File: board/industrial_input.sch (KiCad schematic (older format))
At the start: 3 parts

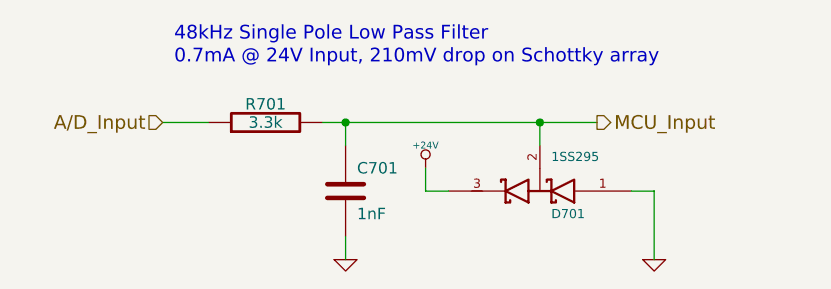
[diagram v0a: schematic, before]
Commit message: Selected Part Numbers for all Components
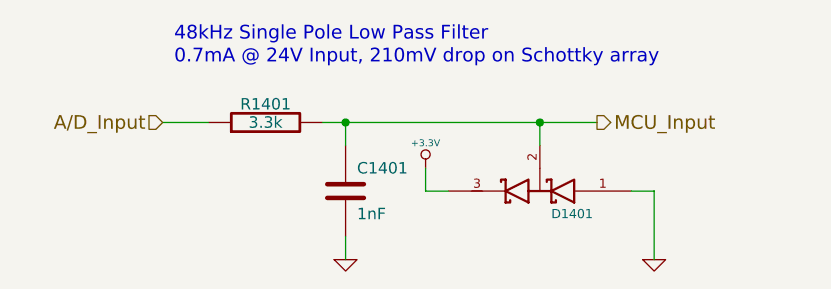
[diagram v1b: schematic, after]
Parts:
- C701: Part Number (none) -> CL10B102KB8NCNC
- D701: Part Number (none) -> 1SS295
- R701: Part Number (none) -> MCR50JZHJ332
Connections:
- net +24V renamed +3.3V
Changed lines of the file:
@@
 AR Path="/52F88315/52E6DE87" Ref="R1301"  Part="1"
 AR Path="/52F88319/52E6DE87" Ref="R1401"  Part="1"
-F 0 "R701" V 5480 3950 50  0000 C CNN
+F 0 "R1401" V 5480 3950 50  0000 C CNN
 F 1 "3.3k" V 5400 3950 50  0000 C CNN
 F 2 "" H 5400 3950 60  0000 C CNN
 F 3 "" H 5400 3950 60  0000 C CNN
+F 4 "MCR50JZHJ332" V 5400 3950 60  0001 C CNN "Part Number"
 	1    5400 3950
 	0    -1   -1   0
@@
 AR Path="/52F88315/52E6DEAB" Ref="C1301"  Part="1"
 AR Path="/52F88319/52E6DEAB" Ref="C1401"  Part="1"
-F 0 "C701" H 5800 4350 50  0000 L CNN
+F 0 "C1401" H 5800 4350 50  0000 L CNN
 F 1 "1nF" H 5800 4150 50  0000 L CNN
 F 2 "" H 5750 4250 60  0000 C CNN
 F 3 "" H 5750 4250 60  0000 C CNN
+F 4 "CL10B102KB8NCNC" H 5750 4250 60  0001 C CNN "Part Number"
 	1    5750 4250
 	1    0    0    -1
 $EndComp
 $Comp
-L GND #PWR0136
+L GND #PWR0141
 U 1 1 52E6DEC4
 P 5750 4550
-AR Path="/52F84966/52E6DEC4" Ref="#PWR0136"  Part="1"
-AR Path="/52F85705/52E6DEC4" Ref="#PWR0139"  Part="1"
-AR Path="/52F85B83/52E6DEC4" Ref="#PWR0142"  Part="1"
-AR Path="/52F85B87/52E6DEC4" Ref="#PWR0145"  Part="1"
-AR Path="/52F8830D/52E6DEC4" Ref="#PWR0148"  Part="1"
-AR Path="/52F88311/52E6DEC4" Ref="#PWR0151"  Part="1"
-AR Path="/52F88315/52E6DEC4" Ref="#PWR0154"  Part="1"
-AR Path="/52F88319/52E6DEC4" Ref="#PWR0157"  Part="1"
-F 0 "#PWR0136" H 5750 4550 30  0001 C CNN
+AR Path="/52F84966/52E6DEC4" Ref="#PWR0141"  Part="1"
+AR Path="/52F85705/52E6DEC4" Ref="#PWR0144"  Part="1"
+AR Path="/52F85B83/52E6DEC4" Ref="#PWR0147"  Part="1"
+AR Path="/52F85B87/52E6DEC4" Ref="#PWR0150"  Part="1"
+AR Path="/52F8830D/52E6DEC4" Ref="#PWR0153"  Part="1"
+AR Path="/52F88311/52E6DEC4" Ref="#PWR0156"  Part="1"
+AR Path="/52F88315/52E6DEC4" Ref="#PWR0159"  Part="1"
+AR Path="/52F88319/52E6DEC4" Ref="#PWR0162"  Part="1"
+F 0 "#PWR0162" H 5750 4550 30  0001 C CNN
 F 1 "GND" H 5750 4480 30  0001 C CNN
 F 2 "" H 5750 4550 60  0000 C CNN
@@
 $EndComp
 $Comp
-L +24V #PWR0137
-U 1 1 52E6DFBF
-P 6100 4150
-AR Path="/52F84966/52E6DFBF" Ref="#PWR0137"  Part="1"
-AR Path="/52F85705/52E6DFBF" Ref="#PWR0140"  Part="1"
-AR Path="/52F85B83/52E6DFBF" Ref="#PWR0143"  Part="1"
-AR Path="/52F85B87/52E6DFBF" Ref="#PWR0146"  Part="1"
-AR Path="/52F8830D/52E6DFBF" Ref="#PWR0149"  Part="1"
-AR Path="/52F88311/52E6DFBF" Ref="#PWR0152"  Part="1"
-AR Path="/52F88315/52E6DFBF" Ref="#PWR0155"  Part="1"
-AR Path="/52F88319/52E6DFBF" Ref="#PWR0158"  Part="1"
-F 0 "#PWR0137" H 6100 4100 20  0001 C CNN
-F 1 "+24V" H 6100 4250 30  0000 C CNN
-F 2 "" H 6100 4150 60  0000 C CNN
-F 3 "" H 6100 4150 60  0000 C CNN
-	1    6100 4150
-	1    0    0    -1
-$EndComp
-$Comp
-L GND #PWR0138
+L GND #PWR0142
 U 1 1 52E6DFEB
 P 7100 4550
-AR Path="/52F84966/52E6DFEB" Ref="#PWR0138"  Part="1"
-AR Path="/52F85705/52E6DFEB" Ref="#PWR0141"  Part="1"
-AR Path="/52F85B83/52E6DFEB" Ref="#PWR0144"  Part="1"
-AR Path="/52F85B87/52E6DFEB" Ref="#PWR0147"  Part="1"
-AR Path="/52F8830D/52E6DFEB" Ref="#PWR0150"  Part="1"
-AR Path="/52F88311/52E6DFEB" Ref="#PWR0153"  Part="1"
-AR Path="/52F88315/52E6DFEB" Ref="#PWR0156"  Part="1"
-AR Path="/52F88319/52E6DFEB" Ref="#PWR0159"  Part="1"
-F 0 "#PWR0138" H 7100 4550 30  0001 C CNN
+AR Path="/52F84966/52E6DFEB" Ref="#PWR0142"  Part="1"
+AR Path="/52F85705/52E6DFEB" Ref="#PWR0145"  Part="1"
+AR Path="/52F85B83/52E6DFEB" Ref="#PWR0148"  Part="1"
+AR Path="/52F85B87/52E6DFEB" Ref="#PWR0151"  Part="1"
+AR Path="/52F8830D/52E6DFEB" Ref="#PWR0154"  Part="1"
+AR Path="/52F88311/52E6DFEB" Ref="#PWR0157"  Part="1"
+AR Path="/52F88315/52E6DFEB" Ref="#PWR0160"  Part="1"
+AR Path="/52F88319/52E6DFEB" Ref="#PWR0163"  Part="1"
+F 0 "#PWR0163" H 7100 4550 30  0001 C CNN
 F 1 "GND" H 7100 4480 30  0001 C CNN
 F 2 "" H 7100 4550 60  0000 C CNN
@@
 AR Path="/52F88315/52E6E5BB" Ref="D1301"  Part="1"
 AR Path="/52F88319/52E6E5BB" Ref="D1401"  Part="1"
-F 0 "D701" H 6550 4350 40  0000 R CNN
-F 1 "1SS295" H 6550 4100 40  0000 R CNN
+F 0 "D1401" H 6550 4350 40  0000 R CNN
+F 1 "1SS295" H 6550 4100 40  0001 R CNN
 F 2 "" H 6600 4250 60  0000 C CNN
 F 3 "" H 6600 4250 60  0000 C CNN
+F 4 "1SS295" H 6600 4250 60  0001 C CNN "Part Number"
 	1    6600 4250
 	-1   0    0    1
@@
 Text Notes 5000 3700 0    60   ~ 0
 0.7mA @ 24V Input, 210mV drop on Schottky array
+$Comp
+L +3.3V #PWR0143
+U 1 1 5301839B
+P 6100 4150
+AR Path="/52F84966/5301839B" Ref="#PWR0143"  Part="1"
+AR Path="/52F85705/5301839B" Ref="#PWR0146"  Part="1"
+AR Path="/52F85B83/5301839B" Ref="#PWR0149"  Part="1"
+AR Path="/52F85B87/5301839B" Ref="#PWR0152"  Part="1"
+AR Path="/52F8830D/5301839B" Ref="#PWR0155"  Part="1"
+AR Path="/52F88311/5301839B" Ref="#PWR0158"  Part="1"
+AR Path="/52F88315/5301839B" Ref="#PWR0161"  Part="1"
+AR Path="/52F88319/5301839B" Ref="#PWR0164"  Part="1"
+F 0 "#PWR0164" H 6100 4110 30  0001 C CNN
+F 1 "+3.3V" H 6100 4260 30  0000 C CNN
+F 2 "" H 6100 4150 60  0000 C CNN
+F 3 "" H 6100 4150 60  0000 C CNN
+	1    6100 4150
+	1    0    0    -1
+$EndComp
 $EndSCHEMATC

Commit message: Digikey Number + Link
Added a digikey part number and link to all components.
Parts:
- C701: Digikey Number (none) -> 1276-1913-1-ND; Part Number CL10B102KB8NCNC -> (none)
- D701: Digikey Number (none) -> 1SS295(TE85LF)CT-ND; Part Number 1SS295 -> (none)
- R701: Digikey Number (none) -> RHM3.3KBGCT-ND; Part Number MCR50JZHJ332 -> (none)
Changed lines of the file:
@@
 F 1 "3.3k" V 5400 3950 50  0000 C CNN
 F 2 "" H 5400 3950 60  0000 C CNN
-F 3 "" H 5400 3950 60  0000 C CNN
-F 4 "MCR50JZHJ332" V 5400 3950 60  0001 C CNN "Part Number"
+F 3 "http://www.digikey.ca/product-detail/en/MCR50JZHJ332/RHM3.3KBGCT-ND/2291227" H 5400 3950 60  0001 C CNN
+F 4 "RHM3.3KBGCT-ND" H 6900 4550 60  0001 C CNN "Digikey Number"
 	1    5400 3950
 	0    -1   -1   0
@@
 F 1 "1nF" H 5800 4150 50  0000 L CNN
 F 2 "" H 5750 4250 60  0000 C CNN
-F 3 "" H 5750 4250 60  0000 C CNN
-F 4 "CL10B102KB8NCNC" H 5750 4250 60  0001 C CNN "Part Number"
+F 3 "http://www.digikey.ca/product-detail/en/CL10B102KB8NCNC/1276-1913-1-ND/3889999" H 5750 4250 60  0001 C CNN
+F 4 "1276-1913-1-ND" H 6900 4550 60  0001 C CNN "Digikey Number"
 	1    5750 4250
 	1    0    0    -1
@@
 F 1 "1SS295" H 6550 4100 40  0001 R CNN
 F 2 "" H 6600 4250 60  0000 C CNN
-F 3 "" H 6600 4250 60  0000 C CNN
-F 4 "1SS295" H 6600 4250 60  0001 C CNN "Part Number"
+F 3 "http://www.digikey.ca/product-detail/en/1SS295(TE85L,F)/1SS295(TE85LF)CT-ND/4304201" H 6600 4250 60  0001 C CNN
+F 4 "1SS295(TE85LF)CT-ND" H 6900 4550 60  0001 C CNN "Digikey Number"
 	1    6600 4250
 	-1   0    0    1

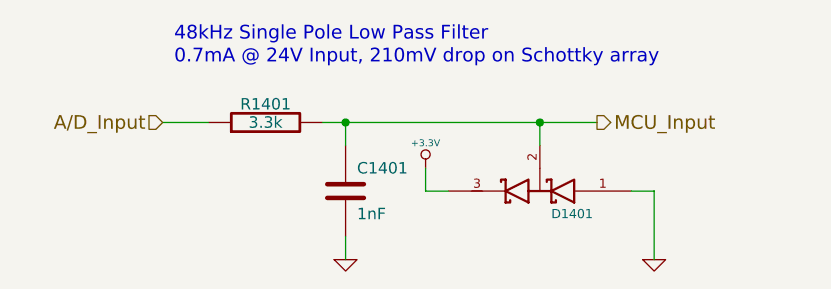
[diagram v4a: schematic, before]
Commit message: Removed PWR-GND, change footprint for a bunch of capacitors
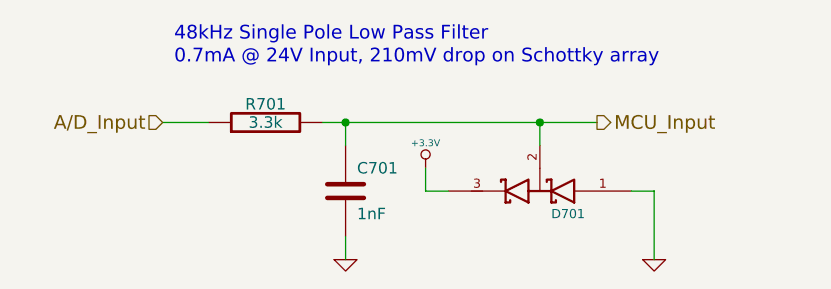
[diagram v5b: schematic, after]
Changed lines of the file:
@@
 AR Path="/52F88315/52E6DE87" Ref="R1301"  Part="1"
 AR Path="/52F88319/52E6DE87" Ref="R1401"  Part="1"
-F 0 "R1401" V 5480 3950 50  0000 C CNN
+F 0 "R701" V 5480 3950 50  0000 C CNN
 F 1 "3.3k" V 5400 3950 50  0000 C CNN
 F 2 "" H 5400 3950 60  0000 C CNN
@@
 AR Path="/52F88315/52E6DEAB" Ref="C1301"  Part="1"
 AR Path="/52F88319/52E6DEAB" Ref="C1401"  Part="1"
-F 0 "C1401" H 5800 4350 50  0000 L CNN
+F 0 "C701" H 5800 4350 50  0000 L CNN
 F 1 "1nF" H 5800 4150 50  0000 L CNN
 F 2 "" H 5750 4250 60  0000 C CNN
@@
 $EndComp
 $Comp
-L GND #PWR0141
+L GND #PWR0140
 U 1 1 52E6DEC4
 P 5750 4550
-AR Path="/52F84966/52E6DEC4" Ref="#PWR0141"  Part="1"
-AR Path="/52F85705/52E6DEC4" Ref="#PWR0144"  Part="1"
-AR Path="/52F85B83/52E6DEC4" Ref="#PWR0147"  Part="1"
-AR Path="/52F85B87/52E6DEC4" Ref="#PWR0150"  Part="1"
-AR Path="/52F8830D/52E6DEC4" Ref="#PWR0153"  Part="1"
-AR Path="/52F88311/52E6DEC4" Ref="#PWR0156"  Part="1"
-AR Path="/52F88315/52E6DEC4" Ref="#PWR0159"  Part="1"
-AR Path="/52F88319/52E6DEC4" Ref="#PWR0162"  Part="1"
-F 0 "#PWR0162" H 5750 4550 30  0001 C CNN
+AR Path="/52F84966/52E6DEC4" Ref="#PWR0140"  Part="1"
+AR Path="/52F85705/52E6DEC4" Ref="#PWR0143"  Part="1"
+AR Path="/52F85B83/52E6DEC4" Ref="#PWR0146"  Part="1"
+AR Path="/52F85B87/52E6DEC4" Ref="#PWR0149"  Part="1"
+AR Path="/52F8830D/52E6DEC4" Ref="#PWR0152"  Part="1"
+AR Path="/52F88311/52E6DEC4" Ref="#PWR0155"  Part="1"
+AR Path="/52F88315/52E6DEC4" Ref="#PWR0158"  Part="1"
+AR Path="/52F88319/52E6DEC4" Ref="#PWR0161"  Part="1"
+F 0 "#PWR0140" H 5750 4550 30  0001 C CNN
 F 1 "GND" H 5750 4480 30  0001 C CNN
 F 2 "" H 5750 4550 60  0000 C CNN
@@
 $EndComp
 $Comp
-L GND #PWR0142
+L GND #PWR0141
 U 1 1 52E6DFEB
 P 7100 4550
-AR Path="/52F84966/52E6DFEB" Ref="#PWR0142"  Part="1"
-AR Path="/52F85705/52E6DFEB" Ref="#PWR0145"  Part="1"
-AR Path="/52F85B83/52E6DFEB" Ref="#PWR0148"  Part="1"
-AR Path="/52F85B87/52E6DFEB" Ref="#PWR0151"  Part="1"
-AR Path="/52F8830D/52E6DFEB" Ref="#PWR0154"  Part="1"
-AR Path="/52F88311/52E6DFEB" Ref="#PWR0157"  Part="1"
-AR Path="/52F88315/52E6DFEB" Ref="#PWR0160"  Part="1"
-AR Path="/52F88319/52E6DFEB" Ref="#PWR0163"  Part="1"
-F 0 "#PWR0163" H 7100 4550 30  0001 C CNN
+AR Path="/52F84966/52E6DFEB" Ref="#PWR0141"  Part="1"
+AR Path="/52F85705/52E6DFEB" Ref="#PWR0144"  Part="1"
+AR Path="/52F85B83/52E6DFEB" Ref="#PWR0147"  Part="1"
+AR Path="/52F85B87/52E6DFEB" Ref="#PWR0150"  Part="1"
+AR Path="/52F8830D/52E6DFEB" Ref="#PWR0153"  Part="1"
+AR Path="/52F88311/52E6DFEB" Ref="#PWR0156"  Part="1"
+AR Path="/52F88315/52E6DFEB" Ref="#PWR0159"  Part="1"
+AR Path="/52F88319/52E6DFEB" Ref="#PWR0162"  Part="1"
+F 0 "#PWR0141" H 7100 4550 30  0001 C CNN
 F 1 "GND" H 7100 4480 30  0001 C CNN
 F 2 "" H 7100 4550 60  0000 C CNN
@@
 AR Path="/52F88315/52E6E5BB" Ref="D1301"  Part="1"
 AR Path="/52F88319/52E6E5BB" Ref="D1401"  Part="1"
-F 0 "D1401" H 6550 4350 40  0000 R CNN
+F 0 "D701" H 6550 4350 40  0000 R CNN
 F 1 "1SS295" H 6550 4100 40  0001 R CNN
 F 2 "" H 6600 4250 60  0000 C CNN
@@
 0.7mA @ 24V Input, 210mV drop on Schottky array
 $Comp
-L +3.3V #PWR0143
+L +3.3V #PWR0142
 U 1 1 5301839B
 P 6100 4150
-AR Path="/52F84966/5301839B" Ref="#PWR0143"  Part="1"
-AR Path="/52F85705/5301839B" Ref="#PWR0146"  Part="1"
-AR Path="/52F85B83/5301839B" Ref="#PWR0149"  Part="1"
-AR Path="/52F85B87/5301839B" Ref="#PWR0152"  Part="1"
-AR Path="/52F8830D/5301839B" Ref="#PWR0155"  Part="1"
-AR Path="/52F88311/5301839B" Ref="#PWR0158"  Part="1"
-AR Path="/52F88315/5301839B" Ref="#PWR0161"  Part="1"
-AR Path="/52F88319/5301839B" Ref="#PWR0164"  Part="1"
-F 0 "#PWR0164" H 6100 4110 30  0001 C CNN
+AR Path="/52F84966/5301839B" Ref="#PWR0142"  Part="1"
+AR Path="/52F85705/5301839B" Ref="#PWR0145"  Part="1"
+AR Path="/52F85B83/5301839B" Ref="#PWR0148"  Part="1"
+AR Path="/52F85B87/5301839B" Ref="#PWR0151"  Part="1"
+AR Path="/52F8830D/5301839B" Ref="#PWR0154"  Part="1"
+AR Path="/52F88311/5301839B" Ref="#PWR0157"  Part="1"
+AR Path="/52F88315/5301839B" Ref="#PWR0160"  Part="1"
+AR Path="/52F88319/5301839B" Ref="#PWR0163"  Part="1"
+F 0 "#PWR0142" H 6100 4110 30  0001 C CNN
 F 1 "+3.3V" H 6100 4260 30  0000 C CNN
 F 2 "" H 6100 4150 60  0000 C CNN

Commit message: Layed out in general where stuff is going to be located.
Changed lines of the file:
@@
 AR Path="/52F88315/52E6DE87" Ref="R1301"  Part="1"
 AR Path="/52F88319/52E6DE87" Ref="R1401"  Part="1"
-F 0 "R701" V 5480 3950 50  0000 C CNN
+F 0 "R1401" V 5480 3950 50  0000 C CNN
 F 1 "3.3k" V 5400 3950 50  0000 C CNN
 F 2 "" H 5400 3950 60  0000 C CNN
@@
 AR Path="/52F88315/52E6DEAB" Ref="C1301"  Part="1"
 AR Path="/52F88319/52E6DEAB" Ref="C1401"  Part="1"
-F 0 "C701" H 5800 4350 50  0000 L CNN
+F 0 "C1401" H 5800 4350 50  0000 L CNN
 F 1 "1nF" H 5800 4150 50  0000 L CNN
 F 2 "" H 5750 4250 60  0000 C CNN
@@
 $EndComp
 $Comp
-L GND #PWR0140
+L GND #PWR702
 U 1 1 52E6DEC4
 P 5750 4550
-AR Path="/52F84966/52E6DEC4" Ref="#PWR0140"  Part="1"
-AR Path="/52F85705/52E6DEC4" Ref="#PWR0143"  Part="1"
-AR Path="/52F85B83/52E6DEC4" Ref="#PWR0146"  Part="1"
-AR Path="/52F85B87/52E6DEC4" Ref="#PWR0149"  Part="1"
-AR Path="/52F8830D/52E6DEC4" Ref="#PWR0152"  Part="1"
-AR Path="/52F88311/52E6DEC4" Ref="#PWR0155"  Part="1"
-AR Path="/52F88315/52E6DEC4" Ref="#PWR0158"  Part="1"
-AR Path="/52F88319/52E6DEC4" Ref="#PWR0161"  Part="1"
-F 0 "#PWR0161" H 5750 4550 30  0001 C CNN
+AR Path="/52F84966/52E6DEC4" Ref="#PWR702"  Part="1"
+AR Path="/52F85705/52E6DEC4" Ref="#PWR802"  Part="1"
+AR Path="/52F85B83/52E6DEC4" Ref="#PWR902"  Part="1"
+AR Path="/52F85B87/52E6DEC4" Ref="#PWR1002"  Part="1"
+AR Path="/52F8830D/52E6DEC4" Ref="#PWR1102"  Part="1"
+AR Path="/52F88311/52E6DEC4" Ref="#PWR1202"  Part="1"
+AR Path="/52F88315/52E6DEC4" Ref="#PWR1302"  Part="1"
+AR Path="/52F88319/52E6DEC4" Ref="#PWR1402"  Part="1"
+F 0 "#PWR1402" H 5750 4550 30  0001 C CNN
 F 1 "GND" H 5750 4480 30  0001 C CNN
 F 2 "" H 5750 4550 60  0000 C CNN
@@
 $EndComp
 $Comp
-L GND #PWR0141
+L GND #PWR703
 U 1 1 52E6DFEB
 P 7100 4550
-AR Path="/52F84966/52E6DFEB" Ref="#PWR0141"  Part="1"
-AR Path="/52F85705/52E6DFEB" Ref="#PWR0144"  Part="1"
-AR Path="/52F85B83/52E6DFEB" Ref="#PWR0147"  Part="1"
-AR Path="/52F85B87/52E6DFEB" Ref="#PWR0150"  Part="1"
-AR Path="/52F8830D/52E6DFEB" Ref="#PWR0153"  Part="1"
-AR Path="/52F88311/52E6DFEB" Ref="#PWR0156"  Part="1"
-AR Path="/52F88315/52E6DFEB" Ref="#PWR0159"  Part="1"
-AR Path="/52F88319/52E6DFEB" Ref="#PWR0162"  Part="1"
-F 0 "#PWR0162" H 7100 4550 30  0001 C CNN
+AR Path="/52F84966/52E6DFEB" Ref="#PWR703"  Part="1"
+AR Path="/52F85705/52E6DFEB" Ref="#PWR803"  Part="1"
+AR Path="/52F85B83/52E6DFEB" Ref="#PWR903"  Part="1"
+AR Path="/52F85B87/52E6DFEB" Ref="#PWR1003"  Part="1"
+AR Path="/52F8830D/52E6DFEB" Ref="#PWR1103"  Part="1"
+AR Path="/52F88311/52E6DFEB" Ref="#PWR1203"  Part="1"
+AR Path="/52F88315/52E6DFEB" Ref="#PWR1303"  Part="1"
+AR Path="/52F88319/52E6DFEB" Ref="#PWR1403"  Part="1"
+F 0 "#PWR1403" H 7100 4550 30  0001 C CNN
 F 1 "GND" H 7100 4480 30  0001 C CNN
 F 2 "" H 7100 4550 60  0000 C CNN
@@
 AR Path="/52F88315/52E6E5BB" Ref="D1301"  Part="1"
 AR Path="/52F88319/52E6E5BB" Ref="D1401"  Part="1"
-F 0 "D701" H 6550 4350 40  0000 R CNN
+F 0 "D1401" H 6550 4350 40  0000 R CNN
 F 1 "1SS295" H 6550 4100 40  0001 R CNN
 F 2 "" H 6600 4250 60  0000 C CNN
@@
 0.7mA @ 24V Input, 210mV drop on Schottky array
 $Comp
-L +3.3V #PWR0142
+L +3.3V #PWR701
 U 1 1 5301839B
 P 6100 4150
-AR Path="/52F84966/5301839B" Ref="#PWR0142"  Part="1"
-AR Path="/52F85705/5301839B" Ref="#PWR0145"  Part="1"
-AR Path="/52F85B83/5301839B" Ref="#PWR0148"  Part="1"
-AR Path="/52F85B87/5301839B" Ref="#PWR0151"  Part="1"
-AR Path="/52F8830D/5301839B" Ref="#PWR0154"  Part="1"
-AR Path="/52F88311/5301839B" Ref="#PWR0157"  Part="1"
-AR Path="/52F88315/5301839B" Ref="#PWR0160"  Part="1"
-AR Path="/52F88319/5301839B" Ref="#PWR0163"  Part="1"
-F 0 "#PWR0163" H 6100 4110 30  0001 C CNN
+AR Path="/52F84966/5301839B" Ref="#PWR701"  Part="1"
+AR Path="/52F85705/5301839B" Ref="#PWR801"  Part="1"
+AR Path="/52F85B83/5301839B" Ref="#PWR901"  Part="1"
+AR Path="/52F85B87/5301839B" Ref="#PWR1001"  Part="1"
+AR Path="/52F8830D/5301839B" Ref="#PWR1101"  Part="1"
+AR Path="/52F88311/5301839B" Ref="#PWR1201"  Part="1"
+AR Path="/52F88315/5301839B" Ref="#PWR1301"  Part="1"
+AR Path="/52F88319/5301839B" Ref="#PWR1401"  Part="1"
+F 0 "#PWR1401" H 6100 4110 30  0001 C CNN
 F 1 "+3.3V" H 6100 4260 30  0000 C CNN
 F 2 "" H 6100 4150 60  0000 C CNN
